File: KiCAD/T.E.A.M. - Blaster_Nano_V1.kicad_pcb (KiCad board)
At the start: 2 copper layers, 55.2 x 35.2 mm, 50 parts, among them J1 USB_C_Receptacle_USB2.0_14P, J2 AKKU, J3 LED, J4 Taster, J5 Speaker, J6 Conn_02x03_Counter_Clockwise, Q1 FS8205A, U1 TP4056-42-ESOP8, U2 DW01A, U3 MT3608, U4 ATMEGA328P-AU, U5 CH340G, U6 DFR0299, Y1 Crystal_GND34, Y2 Crystal_GND34

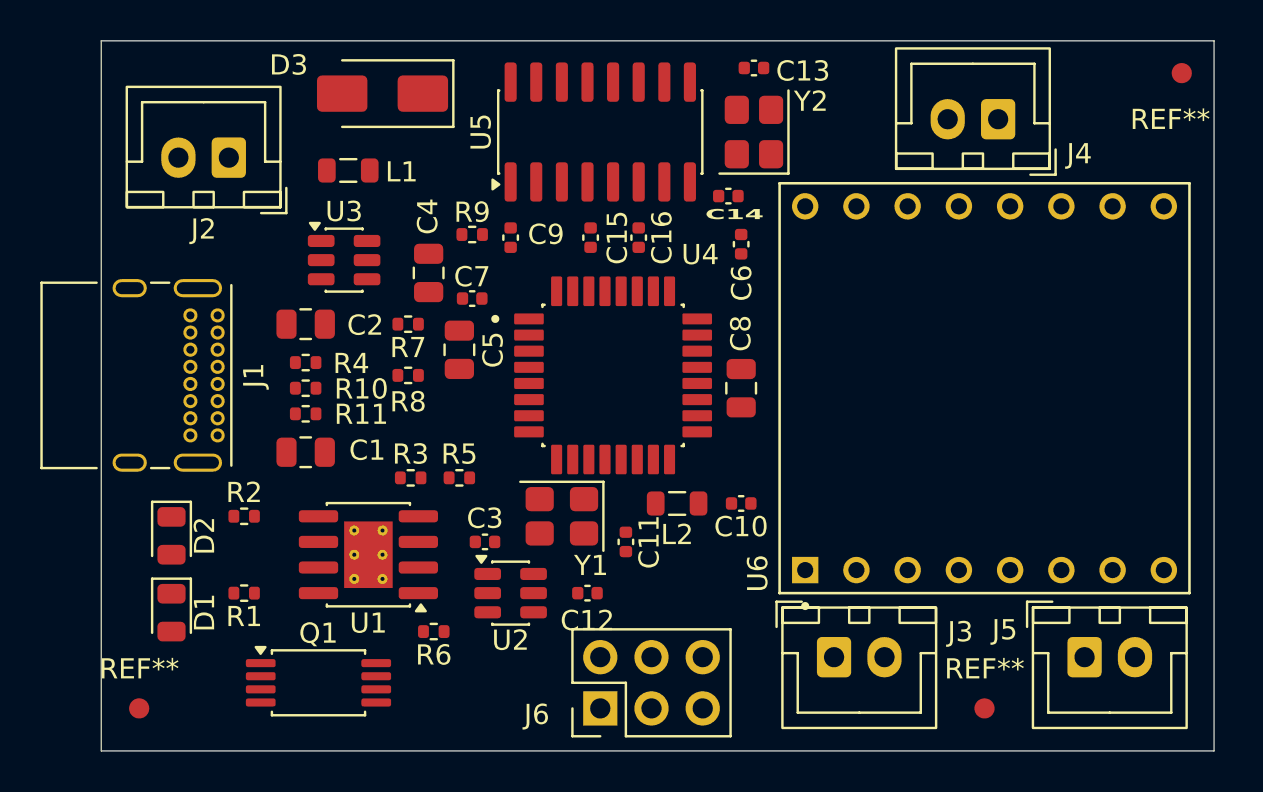
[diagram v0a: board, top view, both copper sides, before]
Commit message: Add GND copper zones on F.Cu and B.Cu
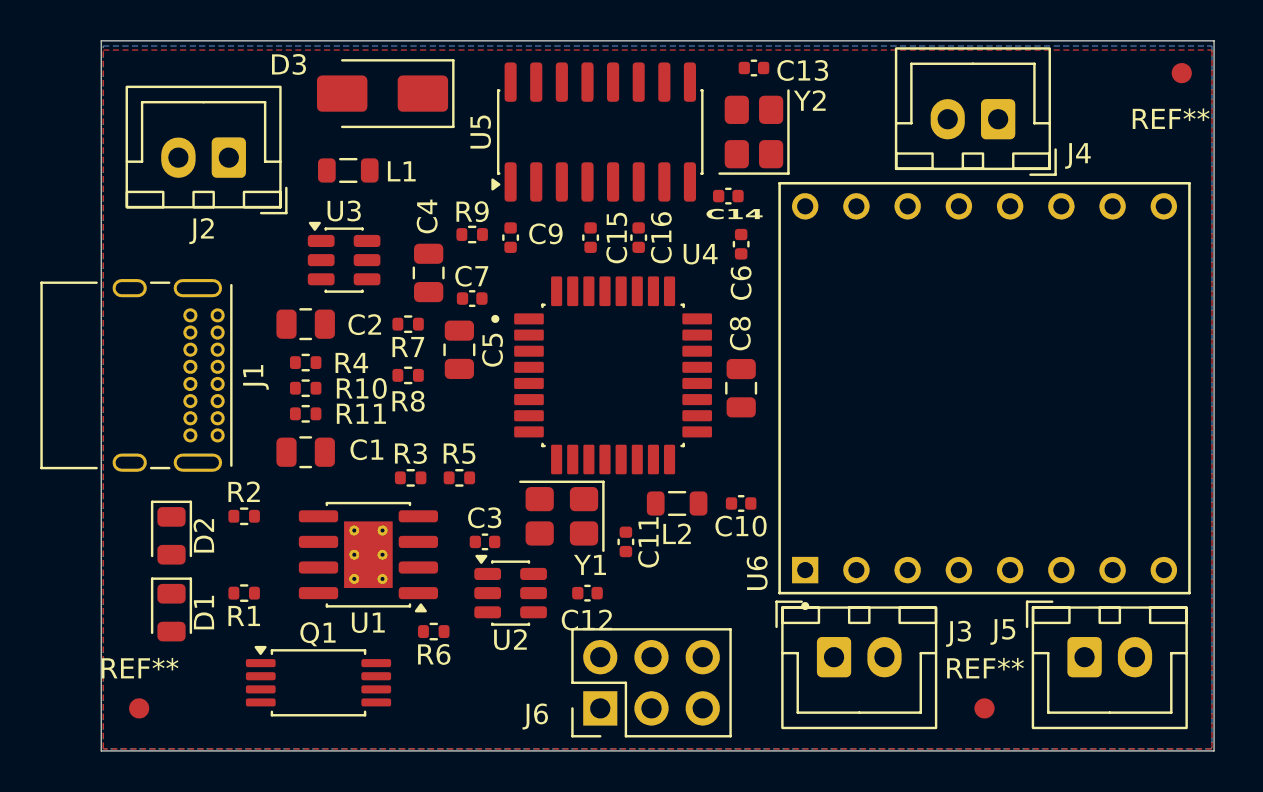
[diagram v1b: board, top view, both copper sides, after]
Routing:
- added copper zone on B.Cu, net GND
- added copper zone on F.Cu, net GND
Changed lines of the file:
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@@
 		(layer "Edge.Cuts")
+	)
+	(zone
+		(net "GND")
+		(layer "F.Cu")
+		(hatch edge 0.5)
+		(connect_pads
+			(clearance 0.2)
+		)
+		(min_thickness 0.25)
+		(fill yes
+			(thermal_gap 0.5)
+			(thermal_bridge_width 0.5)
+			(island_removal_mode 0)
+		)
+		(polygon
+			(pts
+				(xy 161.7472 77.851) (xy 161.7726 77.8764) (xy 161.7726 112.4966) (xy 106.8324 112.4966) (xy 106.807 112.4712)
+				(xy 106.807 77.851)
+			)
+		)
+	)
+	(zone
+		(net "GND")
+		(layer "B.Cu")
+		(hatch edge 0.5)
+		(priority 1)
+		(connect_pads
+			(clearance 0.2)
+		)
+		(min_thickness 0.25)
+		(fill yes
+			(thermal_gap 0.5)
+			(thermal_bridge_width 0.5)
+			(island_removal_mode 0)
+		)
+		(polygon
+			(pts
+				(xy 161.7726 77.6478) (xy 161.7726 112.4458) (xy 161.7218 112.4966) (xy 106.807 112.4966) (xy 106.807 77.6478)
+			)
+		)
 	)
 	(embedded_fonts no)

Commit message: PCB Routing Zwischenstand
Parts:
- removed REF** (x3): Fiducial_1mm_Mask2mm, Fiducial:Fiducial_1mm_Mask2mm
- J2: value AKKU -> Akku
- moved J4 58.2 mm to (106.6, 118.7)
- moved C13 57.7 mm to (84.0, 95.9)
- moved Y2 53.8 mm to (87.3, 96.5), turned to 180 degrees
- moved C14 48.4 mm to (90.7, 95.9), turned to 180 degrees
- moved C15 46.5 mm to (84.5, 88.3)
- moved J3 46.5 mm to (97.8, 118.7), turned to 180 degrees
- moved U5 43.1 mm to (88.9, 88.8), turned to 0 degrees
- moved J2 43.0 mm to (88.9, 118.7)
- moved C10 37.8 mm to (106.0, 80.8), turned to -90 degrees
- moved R11 37.5 mm to (79.4, 95.8), turned to -90 degrees
- moved C16 35.4 mm to (97.9, 88.9), turned to 0 degrees
- moved R4 34.5 mm to (88.9, 113.7), turned to -90 degrees
- moved U1 34.4 mm to (85.6, 105.4)
- moved R10 34.3 mm to (83.8, 85.2), turned to 90 degrees
- moved C1 33.8 mm to (83.2, 100.3), turned to 90 degrees
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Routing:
- net VCC: track 0.00 -> 162.8 mm
- net VBATT: track 0.00 -> 98.5 mm
- net /RESET: track 0.00 -> 48.9 mm, vias 0 -> 1
- net /MCU_TX: track 0.00 -> 20.6 mm, vias 0 -> 2
- net /MCU_RX: track 0.00 -> 18.8 mm, vias 0 -> 2
- net GND: track 0.00 -> 8.49 mm
- net Net-(J1-CC2): track 0.00 -> 8.25 mm, vias 0 -> 1
- net /USB_DM: track 0.00 -> 6.52 mm
- net /USB_DP: track 0.00 -> 6.34 mm
- net Net-(J1-CC1): track 0.00 -> 2.64 mm
- removed copper zone on B.Cu, net GND
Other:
- board size 55.2 x 35.2 mm -> 100.2 x 60 mm
